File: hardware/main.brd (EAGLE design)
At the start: 91 x 58.5 mm, 41 parts, among them U1 TMS320F28069_PN_80, U10 TXB0101_DBV_6, U2 TXB0101_DBV_6, U3 SN74ABT541B_DW_20, U4 SN74LVC1G04_DBV_5, U5 SN74LVC4245A_DW_24, U7 Value, U8 Value, U9 SN74LVC4245A_DW_24

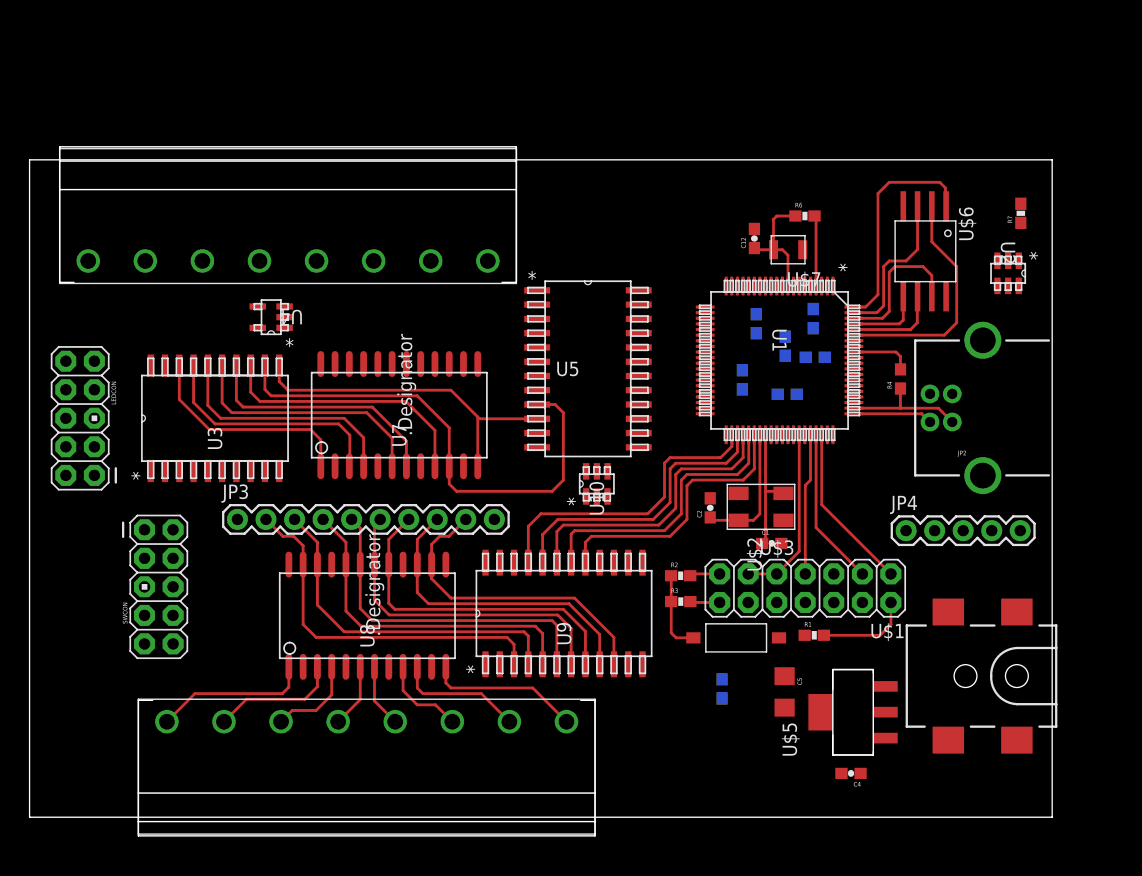
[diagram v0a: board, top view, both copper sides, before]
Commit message: Changed ribbon cable connectors to components on the board. Added DIP switch, LED's. Re-arranged components, started routing.
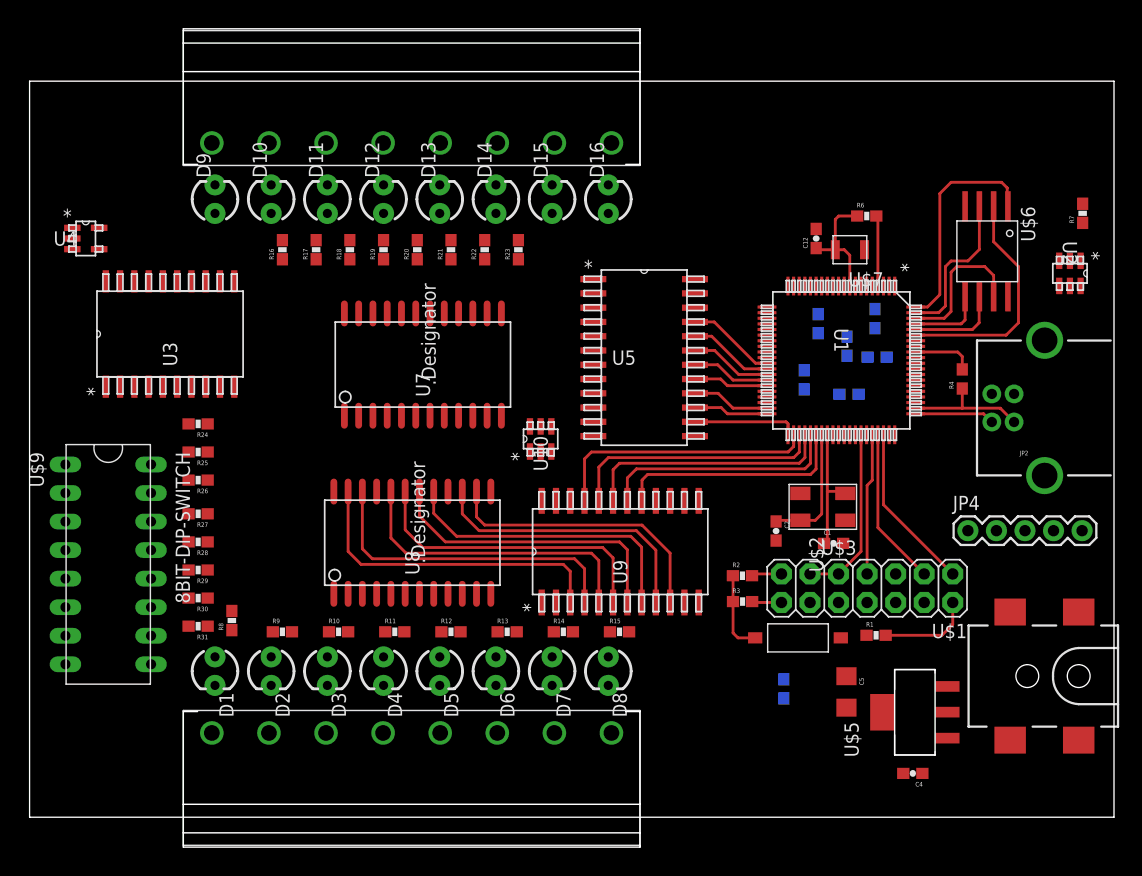
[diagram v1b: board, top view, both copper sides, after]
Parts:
- removed JP3: M10SILK_FEMALE_PTH, SparkFun-Connectors:1X10
- removed LEDCON, SWCON: M05X2PTH, SparkFun-Connectors:AVR_ICSP
- added D1, D10, D11, D12, D13, D14, D15, D16, D2, D3, D4, D5, D6, D7, D8, D9: (no value), SparkFun-LED:LED3MM
- added R10, R11, R12, R13, R14, R15, R16, R17, R18, R19, R20, R21, R22, R23, R8, R9: 240, SparkFun-Resistors:0603-RES
- added R24, R25, R26, R27, R28, R29, R30, R31: 10K, SparkFun-Resistors:0603-RES
- added U$9: 8BIT-DIP-SWITCH, ControllerCard:SPST-DIPS-SW
- moved U4 17.9 mm to (5.00, 51.5), turned to 0 degrees
- moved U$8 15.2 mm to (34.0, 60.0)
- moved U3 8.50 mm to (12.5, 43.0)
- moved U8 7.63 mm to (34.1, 24.4)
- moved U9 7.43 mm to (52.6, 23.6)
- moved U10 6.40 mm to (45.5, 33.7)
- moved C2 6.21 mm to (66.4, 25.5), turned to 270 degrees
- moved C6 5.50 mm to (67.1, 11.4)
- moved C7 5.50 mm to (68.9, 38.9)
- moved C1 5.50 mm to (71.5, 24.4)
- moved C10 5.50 mm to (72.9, 37.6)
- moved C11 5.50 mm to (70.2, 43.9)
- moved C12 5.50 mm to (70.0, 51.5)
- moved C4 5.50 mm to (78.6, 3.90)
- moved C5 5.50 mm to (72.7, 11.2)
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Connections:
- removed net IBUFOUT1: LEDCON.1, U3.18, U5.3, U7.1
- removed net IBUFOUT2: LEDCON.3, U3.17, U5.4, U7.3
- removed net IBUFOUT3: LEDCON.5, U3.16, U5.5, U7.4
- removed net IBUFOUT4: LEDCON.7, U3.15, U5.6, U7.6
- removed net IBUFOUT5: LEDCON.2, U3.14, U5.7, U7.7
- removed net IBUFOUT6: LEDCON.4, U3.13, U5.8, U7.9
- removed net IBUFOUT7: LEDCON.6, U3.12, U5.9, U7.10
- removed net IBUFOUT8: LEDCON.8, U3.11, U5.10, U7.12
- removed net N$29: SWCON.1, U3.2
- new net LEDIN1: R16.2, U3.18, U5.3, U7.1
- new net LEDIN2: R17.2, U3.17, U5.4, U7.3
- new net LEDIN3: R18.2, U3.16, U5.5, U7.4
- new net LEDIN4: R19.2, U3.15, U5.6, U7.6
- new net LEDIN5: R20.2, U3.14, U5.7, U7.7
- new net LEDIN6: R21.2, U3.13, U5.8, U7.9
- new net LEDIN7: R22.2, U3.12, U5.9, U7.10
- new net LEDIN8: R23.2, U3.11, U5.10, U7.12
- new net LEDOUT1: R8.2, U8.23, U9.3
- new net LEDOUT2: R9.2, U8.22, U9.4
- new net LEDOUT3: R10.2, U8.20, U9.5
- new net LEDOUT4: R11.2, U8.19, U9.6
- new net LEDOUT5: R12.2, U8.18, U9.7
- new net LEDOUT6: R13.2, U8.17, U9.8
- new net LEDOUT7: R14.2, U8.15, U9.9
- new net LEDOUT8: R15.2, U8.14, U9.10
- new net SW1: R24.2, U$9.1, U3.2
- new net SW2: R25.2, U$9.2, U3.3
- new net SW3: R26.2, U$9.3, U3.4
- new net SW4: R27.2, U$9.4, U3.5
- new net SW5: R28.2, U$9.5, U3.6
- new net SW6: R29.2, U$9.6, U3.7
- new net SW7: R30.2, U$9.7, U3.8
- new net SW8: R31.2, U$9.8, U3.9
- net 5V: now also U$9.10, U$9.11, U$9.12, U$9.13, U$9.14, U$9.15, U$9.16, U$9.9; no longer JP3.10, LEDCON.9, SWCON.9
- net GND: now also D1.K, D10.K, D11.K, D12.K, D13.K, D14.K, D15.K, D16.K, D2.K, D3.K, D4.K, D5.K, D6.K, D7.K, D8.K, D9.K, R24.1, R25.1, R26.1, R27.1, R28.1, R29.1, R30.1, R31.1; no longer JP3.1, LEDCON.10
- net N$10: now also D6.A, R13.1; no longer JP3.8, U8.15, U9.9
- net N$11: now also D7.A, R14.1; no longer JP3.7, U8.17, U9.8
- net N$12: now also D8.A, R15.1; no longer JP3.6, U8.18, U9.7
- net N$30: now also D9.A, R16.1; no longer SWCON.3, U3.3
- net N$31: now also D10.A, R17.1; no longer SWCON.5, U3.4
- net N$32: now also D11.A, R18.1; no longer SWCON.7, U3.5
- net N$33: now also D12.A, R19.1; no longer SWCON.2, U3.6
- net N$34: now also D13.A, R20.1; no longer SWCON.4, U3.7
- net N$35: now also D14.A, R21.1; no longer SWCON.6, U3.8
- net N$36: now also D15.A, R22.1; no longer SWCON.10
- net N$37: now also D16.A, R23.1; no longer SWCON.8, U3.9
- net N$5: now also D1.A, R8.1; no longer JP3.2, U8.23, U9.3
- net N$6: now also D2.A, R9.1; no longer JP3.3, U8.22, U9.4
- net N$7: now also D3.A, R10.1; no longer JP3.4, U8.20, U9.5
- net N$8: now also D4.A, R11.1; no longer JP3.5, U8.19, U9.6
- net N$9: now also D5.A, R12.1; no longer JP3.9, U8.14, U9.10
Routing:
- net IBUFOUT7: track 44.4 -> 0.00 mm
- net N$5: track 32.6 -> 0.00 mm
- net N$6: track 30.9 -> 0.00 mm
- net IBUFOUT8: track 30.1 -> 0.00 mm
- net N$7: track 30.1 -> 0.00 mm
- net N$8: track 29.8 -> 0.00 mm
- net N$11: track 29.7 -> 0.00 mm
- net N$12: track 29.1 -> 0.00 mm
- net LEDOUT1: track 0.00 -> 28.6 mm
- net LEDOUT2: track 0.00 -> 28.6 mm
- net N$9: track 27.8 -> 0.00 mm
- net N$10: track 27.7 -> 0.00 mm
- net LEDOUT3: track 0.00 -> 27.2 mm
- net LEDOUT4: track 0.00 -> 26.9 mm
- net LEDOUT6: track 0.00 -> 26.6 mm
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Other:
- board size 91 x 58.5 mm -> 96.5 x 65.5 mm

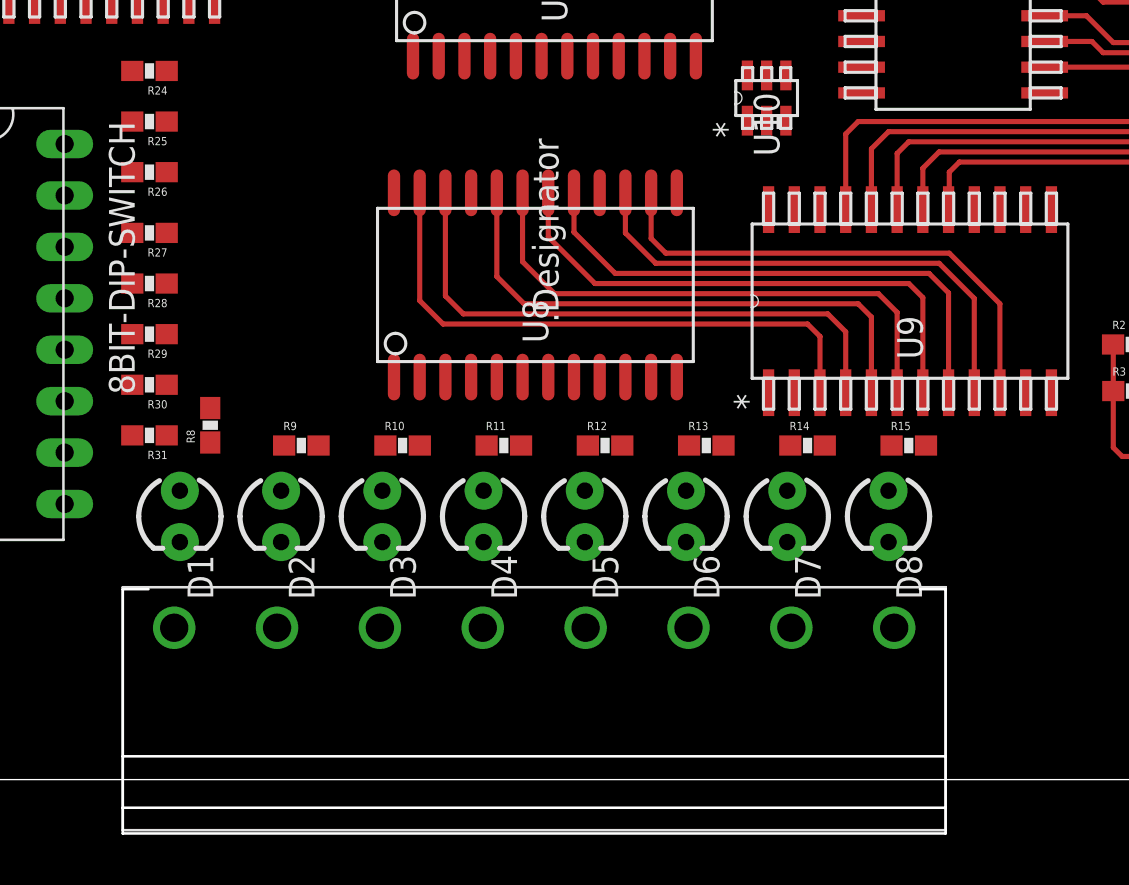
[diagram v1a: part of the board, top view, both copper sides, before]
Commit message: Routed part of output LED section
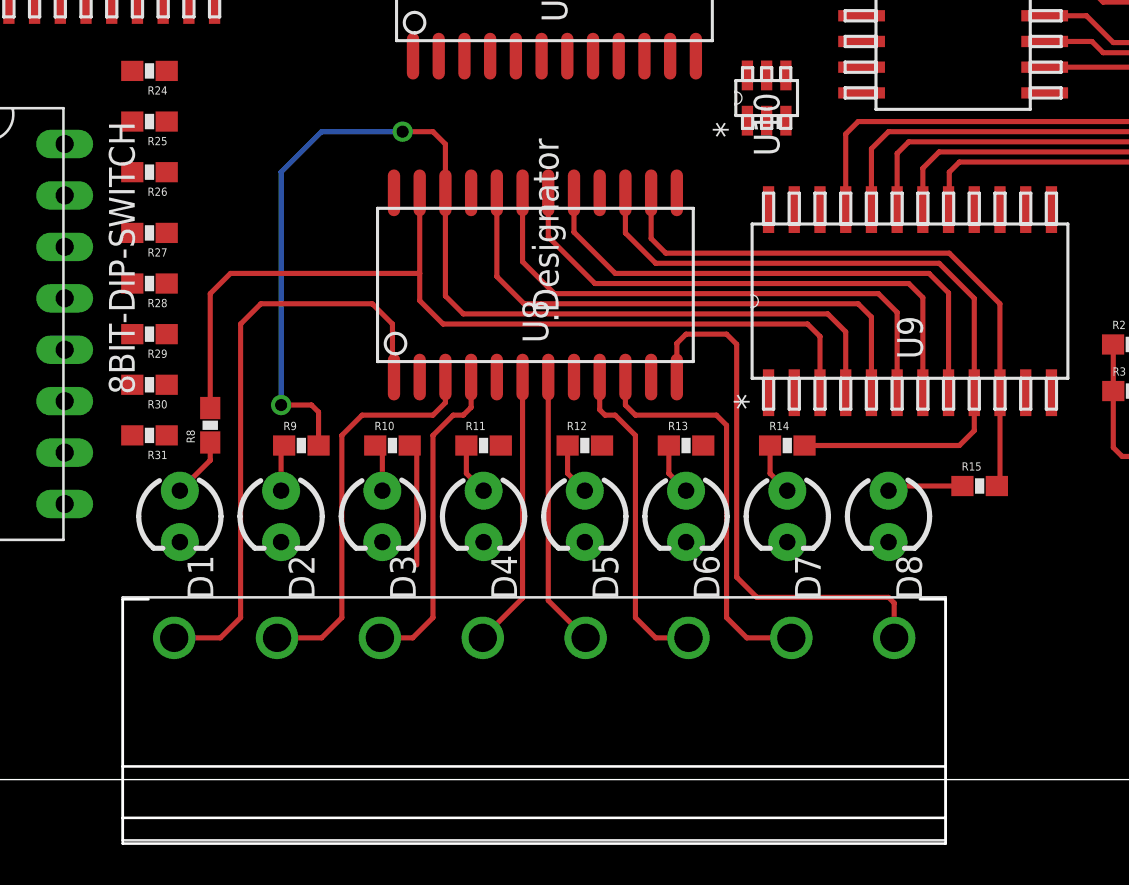
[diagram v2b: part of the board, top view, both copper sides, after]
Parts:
- moved R15 4.03 mm to (56.0, 14.5)
- moved R11 1.00 mm to (31.5, 16.5)
- moved R12 1.00 mm to (36.5, 16.5)
- moved R13 1.00 mm to (41.5, 16.5)
- moved R14 1.00 mm to (46.5, 16.5)
- moved R10 0.50 mm to (27.0, 16.5)
- moved U$4 0.50 mm to (34.0, 7.00)
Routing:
- net N$13: track 0.00 -> 29.2 mm
- net LEDOUT2: track 28.6 -> 55.4 mm, vias 0 -> 2
- net N$17: track 0.00 -> 26.5 mm
- net N$18: track 0.00 -> 19.9 mm
- net N$14: track 0.00 -> 19.7 mm
- net LEDOUT1: track 28.6 -> 45.0 mm
- net N$15: track 0.00 -> 16.0 mm
- net N$19: track 0.00 -> 15.9 mm
- net N$16: track 0.00 -> 13.7 mm
- net N$20: track 0.00 -> 13.6 mm
- net LEDOUT7: track 25.2 -> 35.8 mm
- net LEDOUT3: track 27.2 -> 33.2 mm
- net LEDOUT8: track 25.2 -> 29.9 mm
- net N$12: track 0.00 -> 3.75 mm
- net N$5: track 0.00 -> 3.00 mm
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
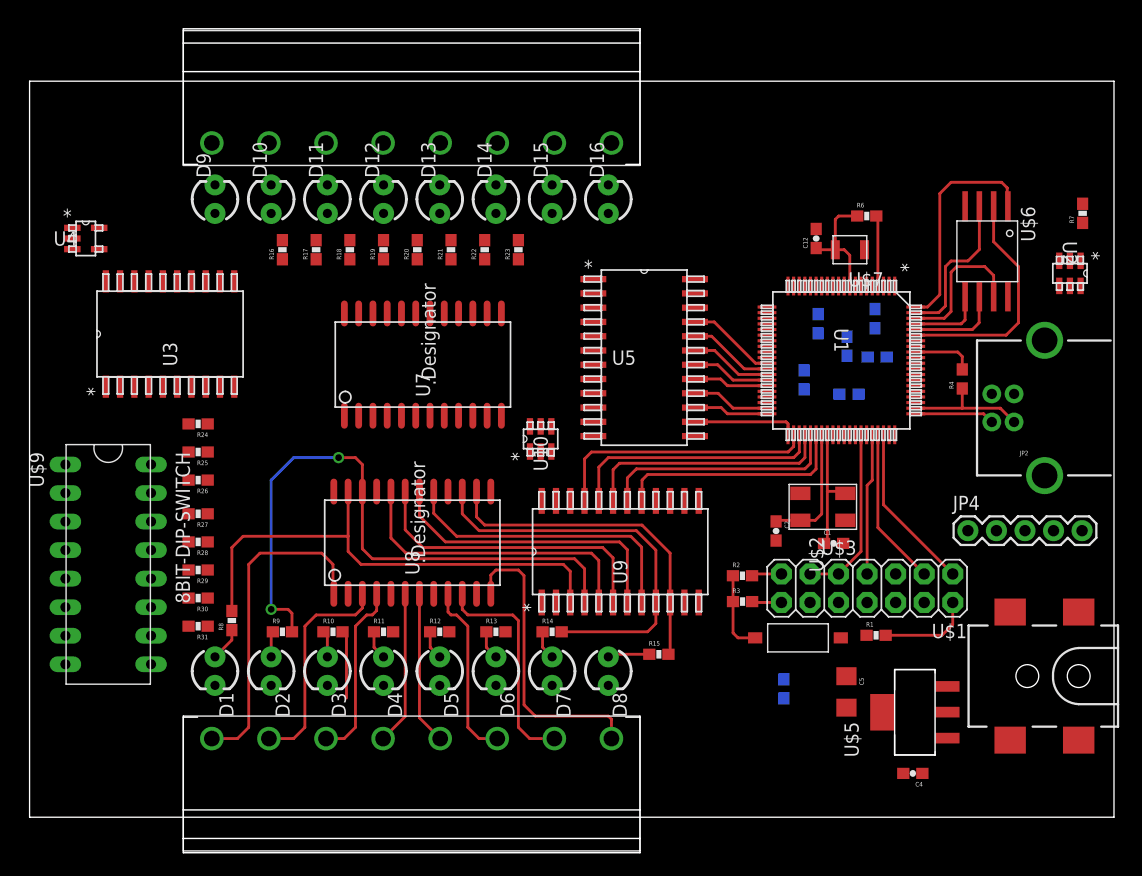
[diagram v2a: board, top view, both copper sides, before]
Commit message: Routed the output section. Ripped up SPI section. Finished routing input section.
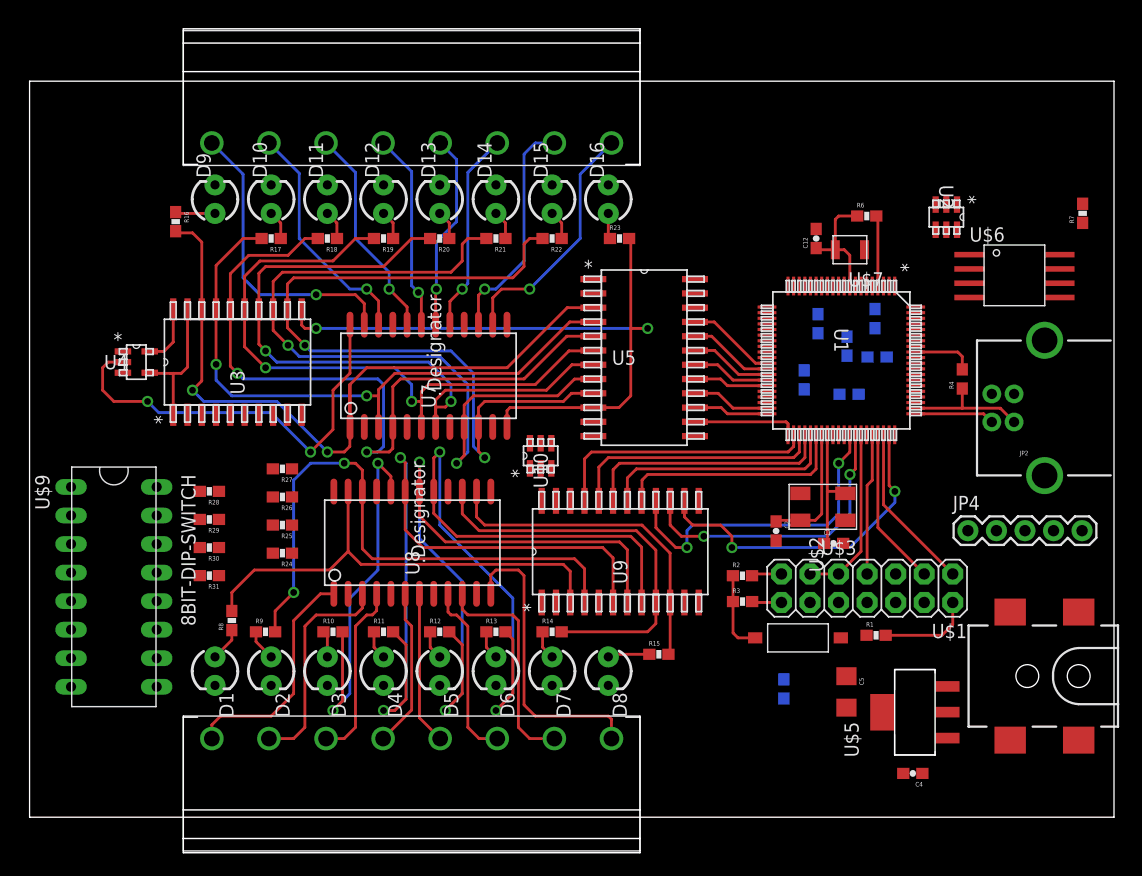
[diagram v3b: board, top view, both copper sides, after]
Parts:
- moved R24 13.7 mm to (22.5, 23.5)
- moved U2 12.1 mm to (81.6, 53.4)
- moved U4 11.9 mm to (9.50, 40.5)
- moved R25 9.92 mm to (22.5, 26.0)
- moved R16 9.82 mm to (13.0, 53.0), turned to 270 degrees
- moved R23 9.06 mm to (52.5, 51.5), turned to 0 degrees
- moved R27 8.50 mm to (22.5, 31.0)
- moved R26 7.65 mm to (22.5, 28.5)
- moved U3 6.50 mm to (18.5, 40.5)
- moved R22 6.08 mm to (46.5, 51.5), turned to 180 degrees
- moved R28 4.61 mm to (16.0, 29.0)
- moved R29 4.61 mm to (16.0, 26.5)
- moved R30 4.61 mm to (16.0, 24.0)
- moved R31 4.61 mm to (16.0, 21.5)
- moved R17 4.12 mm to (21.5, 51.5), turned to 180 degrees
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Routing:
- net LEDIN7: track 0.00 -> 71.0 mm, vias 0 -> 2
- net LEDIN6: track 0.00 -> 70.4 mm, vias 0 -> 2
- net LEDIN1: track 0.00 -> 66.5 mm, vias 0 -> 2
- net LEDIN3: track 0.00 -> 66.5 mm, vias 0 -> 2
- net LEDIN5: track 0.00 -> 64.0 mm, vias 0 -> 2
- net LEDIN8: track 0.00 -> 60.9 mm, vias 0 -> 2
- net LEDIN4: track 0.00 -> 60.0 mm, vias 0 -> 2
- net LEDIN2: track 0.00 -> 58.0 mm, vias 0 -> 2
- net LEDOUT6: track 26.6 -> 64.6 mm, vias 0 -> 2
- net INSEL: track 0.00 -> 37.6 mm, vias 0 -> 2
- net LEDOUT4: track 26.9 -> 63.1 mm, vias 0 -> 2
- net LEDOUT5: track 26.6 -> 61.6 mm, vias 0 -> 2
- net UCOUT8: track 0.00 -> 29.8 mm, vias 0 -> 2
- net UCOUT6: track 0.00 -> 28.9 mm, vias 0 -> 2
- net N$21: track 0.00 -> 26.8 mm, vias 0 -> 1
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
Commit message: Arranged and began routing DIP switches
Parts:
- moved R24 20.3 mm to (3.00, 18.0), turned to 90 degrees
- moved R25 18.8 mm to (5.50, 18.0), turned to 90 degrees
- moved R26 17.9 mm to (8.00, 18.0), turned to 90 degrees
- moved R27 17.7 mm to (10.5, 18.0), turned to 90 degrees
- moved R30 13.2 mm to (10.5, 12.0), turned to 90 degrees
- moved R28 11.4 mm to (13.0, 18.0), turned to 90 degrees
- moved R31 9.96 mm to (13.0, 12.0), turned to 90 degrees
- moved R29 8.51 mm to (15.5, 18.0), turned to 90 degrees
- moved U$9 7.11 mm to (12.0, 26.0), turned to 0 degrees
- moved C4 5.05 mm to (83.6, 4.60), turned to 270 degrees
- moved C5 4.92 mm to (70.7, 6.65)
- moved U2 3.91 mm to (78.6, 55.9)
- moved U$5 3.73 mm to (77.7, 5.78), turned to 180 degrees
- moved C6 1.29 mm to (65.9, 11.9), turned to 0 degrees
- moved U$6 1.12 mm to (86.6, 48.7)
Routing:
- net SW1: track 0.00 -> 22.8 mm
- net SW6: track 0.00 -> 22.3 mm
- net SW2: track 0.00 -> 21.7 mm
- net SW7: track 0.00 -> 20.3 mm
- net SW3: track 0.00 -> 20.0 mm
- net SW4: track 0.00 -> 19.2 mm
- net SW5: track 0.00 -> 18.9 mm
- net SW8: track 0.00 -> 17.8 mm
- net 5V: track 5.34 -> 23.1 mm
- net LEDOUT1: track 42.1 -> 41.1 mm
